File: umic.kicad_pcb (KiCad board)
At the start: 2 copper layers, 68.6 x 71.1 mm, 32 parts, among them J1 USB_B_Micro, J2 Conn_01x06, SW1 SW_MEC_5G, U1 LP38693MP-3.3, U2 STM32F302RBTx, Y1 32.768kHz, Y2 8MHz

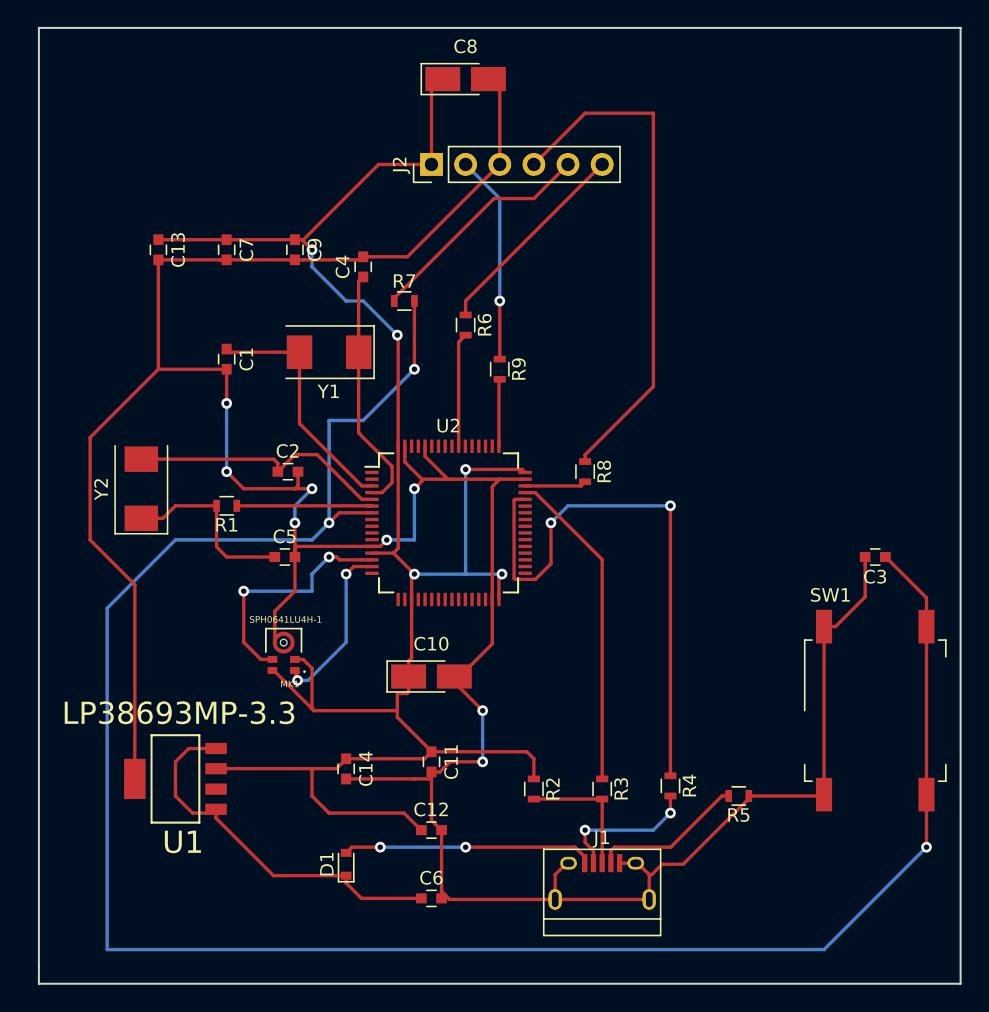
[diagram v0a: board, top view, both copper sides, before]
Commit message: take2: with ground plane
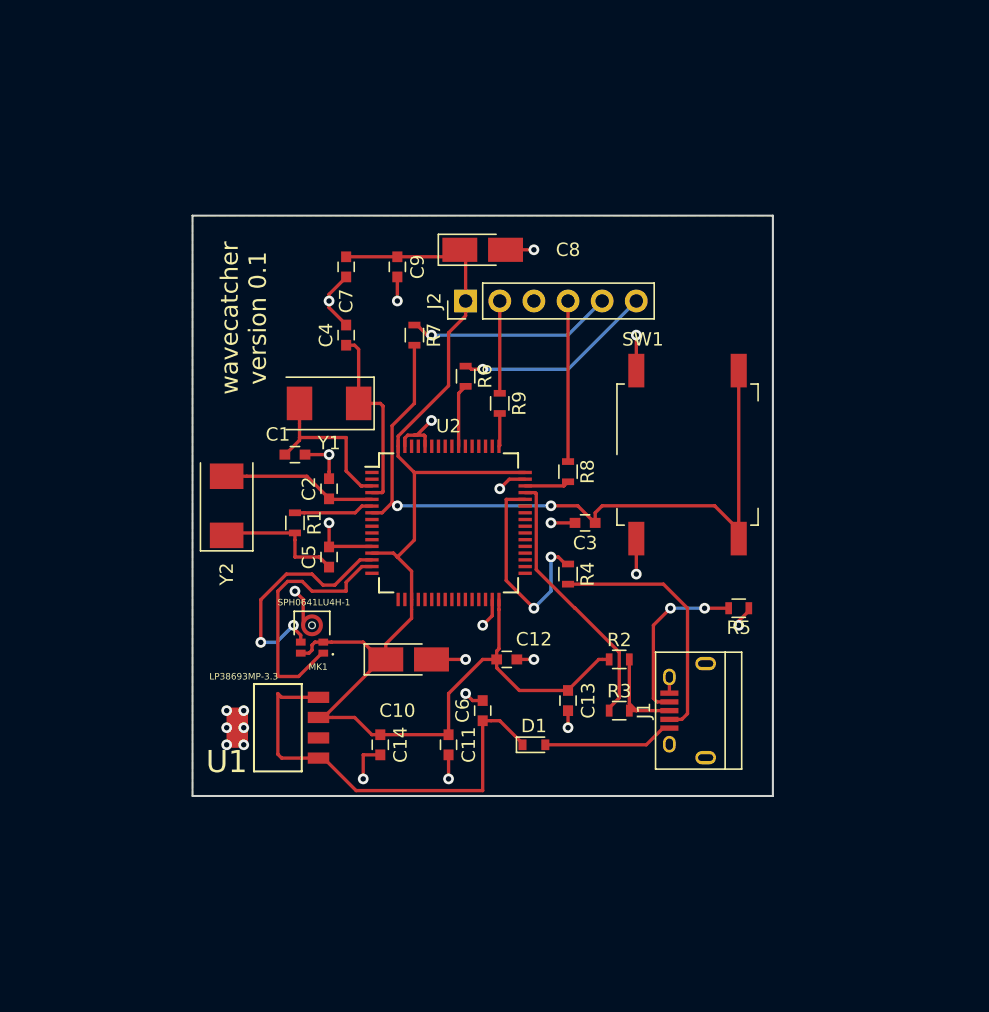
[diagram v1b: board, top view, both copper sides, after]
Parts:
- moved C13 45.3 mm to (57.1, 65.3)
- moved SW1 23.6 mm to (66.0, 47.0)
- moved C3 21.7 mm to (58.4, 52.1)
- moved R4 17.5 mm to (57.1, 55.9)
- moved D1 16.6 mm to (54.6, 68.6), turned to 0 degrees
- moved C6 14.5 mm to (50.8, 66.0), turned to 90 degrees
- moved J1 14.2 mm to (66.0, 66.0), turned to 90 degrees
- moved R5 14.0 mm to (69.8, 58.4)
- moved C12 13.9 mm to (52.6, 62.2)
- moved C8 12.8 mm to (50.8, 31.8)
- moved R2 11.5 mm to (61.0, 62.2), turned to 0 degrees
- moved J2 10.5 mm to (49.5, 35.6)
- moved C7 8.98 mm to (40.6, 33.0)
- moved C1 8.73 mm to (36.8, 47.0), turned to 0 degrees
- moved U1 8.52 mm to (35.6, 67.3)
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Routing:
- net GND: track 242.6 -> 50.3 mm, vias 8 -> 25
- net Net-(C3-Pad1): track 155.7 -> 55.5 mm, vias 3 -> 2
- net VDD: track 149.0 -> 101.2 mm, vias 5 -> 0
- net Net-(J2-Pad4): track 38.5 -> 11.9 mm
- net Net-(R4-Pad1): track 42.5 -> 16.2 mm
- net +5V: track 18.7 -> 9.74 mm, vias 2 -> 0
- net Net-(J2-Pad2): track 15.5 -> 6.87 mm, vias 1 -> 0
- net Net-(C2-Pad1): track 19.8 -> 11.5 mm
- net Net-(J1-Pad2): track 10.9 -> 19.0 mm, vias 2 -> 0
- net Net-(MK1-Pad1): track 13.1 -> 19.2 mm, vias 2 -> 0
- net Net-(C1-Pad1): track 18.1 -> 12.6 mm
- net Net-(C6-Pad1): track 28.4 -> 33.0 mm
- net Net-(R3-Pad1): track 24.1 -> 19.9 mm
- net Net-(R1-Pad1): track 10.1 -> 5.94 mm
- net Net-(C4-Pad1): track 18.3 -> 14.2 mm
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- added copper zone on B.Cu, net GND
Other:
- board size 68.6 x 71.1 mm -> 43.2 x 43.2 mm
- board text added: "wavecatcher version 0.1"

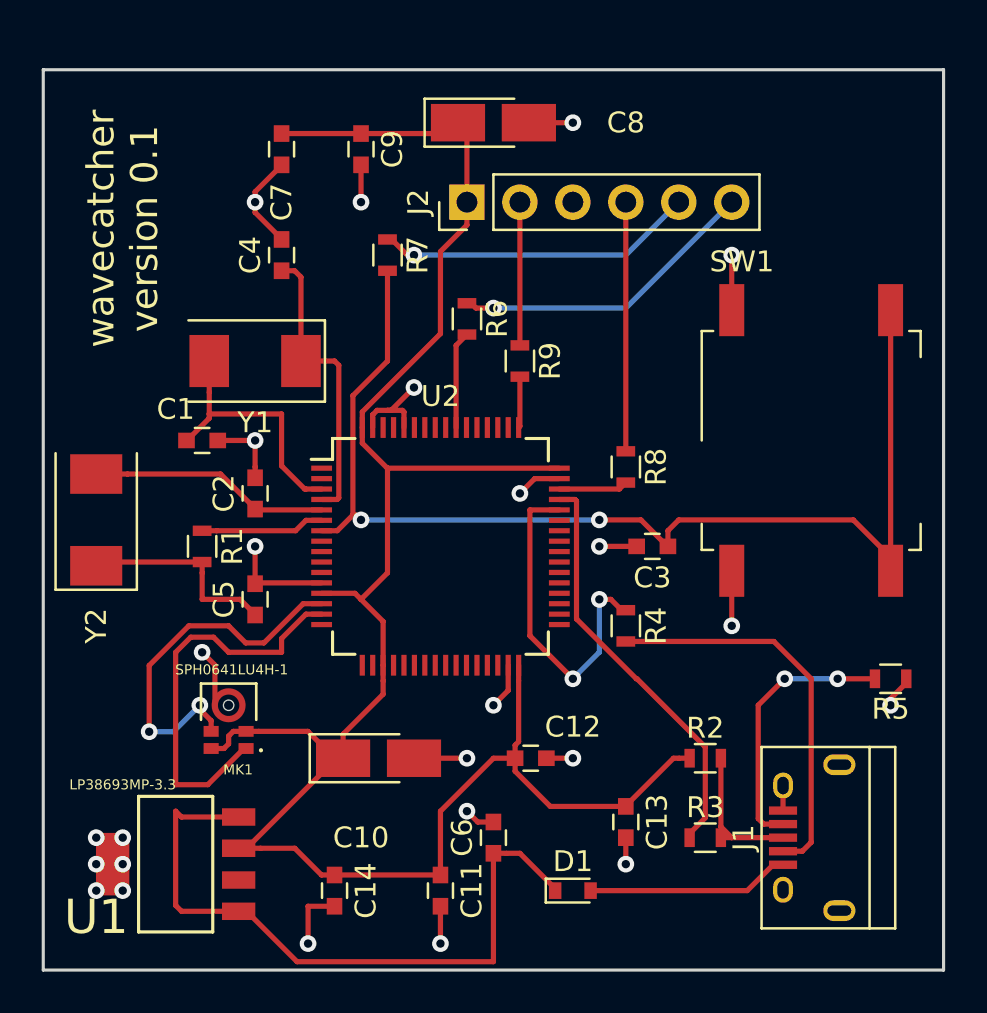
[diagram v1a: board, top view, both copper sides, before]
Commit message: added led
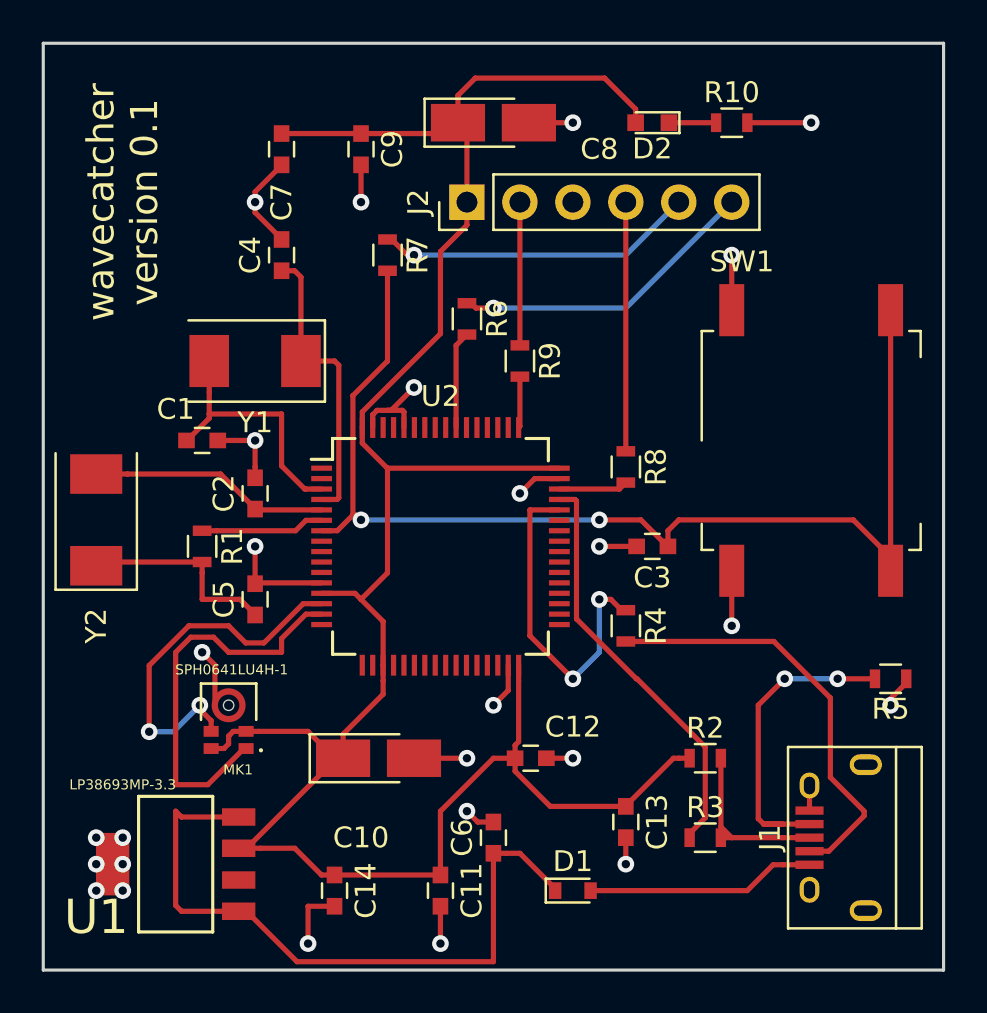
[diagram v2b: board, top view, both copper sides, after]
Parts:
- added D2: LED, LEDs:LED_0603, F.Cu at (58.4, 31.8)
- added R10: 68, Resistors_SMD:R_0603, F.Cu at (62.2, 31.8)
- moved J1 1.27 mm to (67.3, 66.0)
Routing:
- net VDD: track 101.2 -> 112.7 mm
- net GND: track 50.3 -> 53.3 mm, vias 25 -> 26
- net Net-(D2-Pad1): track 0.00 -> 2.26 mm
- net Net-(J1-Pad4): track 12.9 -> 15.1 mm
- net Net-(J1-Pad2): track 19.0 -> 20.6 mm
- net Net-(J1-Pad3): track 7.01 -> 8.28 mm
- net +5V: track 9.74 -> 11.0 mm
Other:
- board size 43.2 x 43.2 mm -> 43.2 x 44.5 mm

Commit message: sent off to fab
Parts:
- J1: footprint Connectors:USB_Micro-B -> Connectors:USB_Micro-B_10103594-0001LF
- Y1: footprint Crystals:Crystal_SMD_0603-2pin_6.0x3.5mm -> Crystals:Crystal_SMD_TXC_9HT11-2pin_2.0x1.2mm
- Y2: footprint Crystals:Crystal_SMD_0603-2pin_6.0x3.5mm -> Crystals:Crystal_SMD_Abracon_ABM3-2pin_5.0x3.2mm
- moved Y1 2.84 mm to (38.1, 40.6)
- moved Y2 1.27 mm to (33.0, 50.8)
- moved J1 0.69 mm to (68.0, 66.0)
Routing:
- net GND: track 53.3 -> 57.1 mm
- net Net-(C4-Pad1): track 14.2 -> 16.9 mm
- net Net-(C1-Pad1): track 12.6 -> 15.3 mm
- net Net-(C5-Pad1): track 9.81 -> 8.48 mm
- net Net-(C2-Pad1): track 11.5 -> 10.2 mm
- net Net-(J1-Pad2): track 20.6 -> 19.7 mm
- net Net-(J1-Pad3): track 8.28 -> 8.82 mm
- net +5V: track 11.0 -> 11.6 mm

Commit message: take2 at submitting to the fab
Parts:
- moved MK1 0.61 mm to (38.7, 59.7)
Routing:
- net Net-(MK1-Pad1): track 19.2 -> 8.50 mm
- net Net-(MK1-Pad4): track 17.8 -> 12.4 mm, vias 2 -> 0
- net VDD: track 112.7 -> 114.4 mm
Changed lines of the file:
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@@
     (thickness 1.6)
     (drawings 5)
-    (tracks 294)
+    (tracks 283)
     (zones 0)
     (modules 34)
@@
   )
   (module SPH0641LU4H-1:MIC_SPH0641LU4H-1 (layer F.Cu)
-    (at 38.1 59.69 180)
+    (at 38.71375 59.7025 180)
     (attr smd)
     (fp_text reference MK1 (at -0.452726 -3.09295 180) (layer F.SilkS)
@@
   (segment (start 39.37 53.86) (end 39.37 52.07) (width 0.25) (layer F.Cu) (net 2))
   (via (at 39.37 52.07) (size 0.8) (drill 0.4) (layers F.Cu B.Cu) (net 2))
-  (segment (start 37.44375 59.7025) (end 37.44375 57.76375) (width 0.25) (layer F.Cu) (net 2))
-  (via (at 36.83 57.15) (size 0.8) (drill 0.4) (layers F.Cu B.Cu) (net 2))
-  (segment (start 37.44375 57.76375) (end 36.83 57.15) (width 0.25) (layer F.Cu) (net 2))
   (via (at 31.75 66.04) (size 0.8) (drill 0.4) (layers F.Cu B.Cu) (net 2))
   (via (at 31.75 67.31) (size 0.8) (drill 0.4) (layers F.Cu B.Cu) (net 2))
@@
   (segment (start 38.5826 69.5706) (end 35.8394 69.5706) (width 0.25) (layer F.Cu) (net 7))
   (segment (start 35.8394 69.5706) (end 35.56 69.2912) (width 0.25) (layer F.Cu) (net 7))
-  (segment (start 39.55 60.942) (end 38.9375 60.942) (width 0.25) (layer F.Cu) (net 8))
-  (segment (start 41.902 60.942) (end 39.55 60.942) (width 0.25) (layer F.Cu) (net 8))
-  (segment (start 43.19 62.23) (end 41.902 60.942) (width 0.25) (layer F.Cu) (net 8))
   (segment (start 43.59 62.23) (end 43.19 62.23) (width 0.25) (layer F.Cu) (net 8))
   (segment (start 43.2816 62.23) (end 43.59 62.23) (width 0.25) (layer F.Cu) (net 8))
@@
   (segment (start 52.01 61.435) (end 52.01 58.52) (width 0.25) (layer F.Cu) (net 8))
   (segment (start 51.84 62.23) (end 51.84 61.605) (width 0.25) (layer F.Cu) (net 8))
-  (segment (start 37.875 61.764) (end 38.1 61.539) (width 0.25) (layer F.Cu) (net 8))
-  (segment (start 37.2625 61.764) (end 37.875 61.764) (width 0.25) (layer F.Cu) (net 8))
-  (segment (start 38.325 60.942) (end 38.9375 60.942) (width 0.25) (layer F.Cu) (net 8))
-  (segment (start 38.1 61.167) (end 38.325 60.942) (width 0.25) (layer F.Cu) (net 8))
-  (segment (start 38.1 61.539) (end 38.1 61.167) (width 0.25) (layer F.Cu) (net 8))
   (segment (start 40.64 32.27) (end 44.45 32.27) (width 0.25) (layer F.Cu) (net 8))
   (segment (start 48.58 32.27) (end 49.1 31.75) (width 0.25) (layer F.Cu) (net 8))
@@
   (segment (start 64.69 66.04) (end 62.23 66.04) (width 0.25) (layer F.Cu) (net 11))
   (segment (start 52.07 42.43) (end 52.07 35.56) (width 0.25) (layer F.Cu) (net 13))
-  (segment (start 38.836 61.764) (end 37.1 63.5) (width 0.25) (layer F.Cu) (net 14))
-  (segment (start 38.9375 61.764) (end 38.836 61.764) (width 0.25) (layer F.Cu) (net 14))
-  (segment (start 37.1 63.5) (end 35.56 63.5) (width 0.25) (layer F.Cu) (net 14))
-  (segment (start 35.56 63.5) (end 35.56 57.15) (width 0.25) (layer F.Cu) (net 14))
-  (segment (start 35.56 57.15) (end 36.285001 56.424999) (width 0.25) (layer F.Cu) (net 14))
-  (segment (start 36.285001 56.424999) (end 37.374999 56.424999) (width 0.25) (layer F.Cu) (net 14))
-  (segment (start 37.374999 56.424999) (end 38.1 57.15) (width 0.25) (layer F.Cu) (net 14))
-  (segment (start 38.1 57.15) (end 40.64 57.15) (width 0.25) (layer F.Cu) (net 14))
-  (segment (start 41.81 55.32) (end 42.56 55.32) (width 0.25) (layer F.Cu) (net 14))
-  (segment (start 40.64 56.49) (end 41.81 55.32) (width 0.25) (layer F.Cu) (net 14))
-  (segment (start 40.64 57.15) (end 40.64 56.49) (width 0.25) (layer F.Cu) (net 14))
   (segment (start 41.67359 54.82) (end 39.7936 56.69999) (width 0.25) (layer F.Cu) (net 15))
   (segment (start 42.56 54.82) (end 41.67359 54.82) (width 0.25) (layer F.Cu) (net 15))
   (segment (start 39.7936 56.69999) (end 38.91999 56.69999) (width 0.25) (layer F.Cu) (net 15))
   (segment (start 38.91999 56.69999) (end 38.1 55.88) (width 0.25) (layer F.Cu) (net 15))
-  (segment (start 36.19359 55.88) (end 34.29 57.78359) (width 0.25) (layer F.Cu) (net 15))
-  (segment (start 38.1 55.88) (end 36.19359 55.88) (width 0.25) (layer F.Cu) (net 15))
-  (segment (start 34.29 57.78359) (end 34.29 60.96) (width 0.25) (layer F.Cu) (net 15))
-  (via (at 34.29 60.96) (size 0.8) (drill 0.4) (layers F.Cu B.Cu) (net 15))
-  (segment (start 37.2625 60.431) (end 36.83 59.9985) (width 0.25) (layer F.Cu) (net 15))
-  (segment (start 37.2625 60.942) (end 37.2625 60.431) (width 0.25) (layer F.Cu) (net 15))
-  (via (at 36.71875 59.69) (size 0.8) (drill 0.4) (layers F.Cu B.Cu) (net 15))
-  (segment (start 36.83 59.9985) (end 36.83 59.80125) (width 0.25) (layer F.Cu) (net 15))
-  (segment (start 36.83 59.80125) (end 36.71875 59.69) (width 0.25) (layer F.Cu) (net 15))
-  (segment (start 35.44875 60.96) (end 34.29 60.96) (width 0.25) (layer B.Cu) (net 15))
-  (segment (start 36.71875 59.69) (end 35.44875 60.96) (width 0.25) (layer B.Cu) (net 15))
   (segment (start 37.53 51.32) (end 36.83 51.32) (width 0.25) (layer F.Cu) (net 16))
   (segment (start 41.81 50.82) (end 41.31 51.32) (width 0.25) (layer F.Cu) (net 16))
@@
   (segment (start 69.62 68.53) (end 69.38 68.77) (width 0.25) (layer F.Cu) (net 2))
   (segment (start 69.62 67) (end 69.62 68.53) (width 0.25) (layer F.Cu) (net 2))
+  (segment (start 38.0575 59.715) (end 38.0575 59.415) (width 0.25) (layer F.Cu) (net 2))
+  (via (at 38.1 57.15) (size 0.8) (drill 0.4) (layers F.Cu B.Cu) (net 2))
+  (segment (start 38.0575 57.1925) (end 38.1 57.15) (width 0.25) (layer F.Cu) (net 2))
+  (segment (start 38.0575 59.715) (end 38.0575 57.1925) (width 0.25) (layer F.Cu) (net 2))
   (segment (start 39.37 50.255) (end 39.37 50.28) (width 0.25) (layer F.Cu) (net 3))
   (segment (start 37.865 48.75) (end 39.37 50.255) (width 0.25) (layer F.Cu) (net 3))
@@
   (segment (start 49.1 30.44002) (end 49.1 31.75) (width 0.25) (layer F.Cu) (net 8))
   (segment (start 49.93001 29.61001) (end 49.1 30.44002) (width 0.25) (layer F.Cu) (net 8))
+  (segment (start 39.54575 60.96) (end 39.55125 60.9545) (width 0.25) (layer F.Cu) (net 8))
+  (segment (start 39.159248 60.96) (end 39.54575 60.96) (width 0.25) (layer F.Cu) (net 8))
+  (segment (start 38.342748 61.7765) (end 39.159248 60.96) (width 0.25) (layer F.Cu) (net 8))
+  (segment (start 37.87625 61.7765) (end 38.342748 61.7765) (width 0.25) (layer F.Cu) (net 8))
+  (segment (start 43.59 62.23) (end 42.04 62.23) (width 0.25) (layer F.Cu) (net 8))
+  (segment (start 37.97775 61.7765) (end 37.87625 61.7765) (width 0.25) (layer F.Cu) (net 8))
+  (segment (start 41.10125 63.16875) (end 42.04 62.23) (width 0.25) (layer F.Cu) (net 8))
+  (segment (start 39.37 63.16875) (end 41.10125 63.16875) (width 0.25) (layer F.Cu) (net 8))
+  (segment (start 39.37 63.16875) (end 37.97775 61.7765) (width 0.25) (layer F.Cu) (net 8))
   (segment (start 64.215 67.34) (end 66.5 67.34) (width 0.25) (layer F.Cu) (net 9))
   (segment (start 63.765 65.39) (end 63.5 65.125) (width 0.25) (layer F.Cu) (net 10))
@@
   (segment (start 67.575 66.69) (end 67.650001 66.614999) (width 0.25) (layer F.Cu) (net 12))
   (segment (start 66.5 66.69) (end 67.575 66.69) (width 0.25) (layer F.Cu) (net 12))
+  (segment (start 40.16375 61.7765) (end 40.64 61.30025) (width 0.25) (layer F.Cu) (net 14))
+  (segment (start 39.55125 61.7765) (end 40.16375 61.7765) (width 0.25) (layer F.Cu) (net 14))
+  (segment (start 41.81 55.32) (end 42.56 55.32) (width 0.25) (layer F.Cu) (net 14))
+  (segment (start 40.64 56.49) (end 41.81 55.32) (width 0.25) (layer F.Cu) (net 14))
+  (segment (start 40.64 61.30025) (end 40.64 56.49) (width 0.25) (layer F.Cu) (net 14))
+  (segment (start 37.87625 60.9545) (end 37.77475 60.9545) (width 0.25) (layer F.Cu) (net 15))
+  (segment (start 37.77475 60.9545) (end 36.83 60.00975) (width 0.25) (layer F.Cu) (net 15))
+  (segment (start 36.83 60.00975) (end 36.83 55.88) (width 0.25) (layer F.Cu) (net 15))
+  (segment (start 36.83 55.88) (end 38.1 55.88) (width 0.25) (layer F.Cu) (net 15))
   (segment (start 60.21 65.84) (end 60.96 65.09) (width 0.25) (layer F.Cu) (net 17))
   (segment (start 60.21 66.04) (end 60.21 65.84) (width 0.25) (layer F.Cu) (net 17))

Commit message: take3, connect mic to spi pins
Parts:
- moved MK1 7.44 mm to (45.7, 62.2)
- moved C10 7.30 mm to (38.1, 61.0), turned to 180 degrees
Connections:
- U2 pad 14: Net-(MK1-Pad4) -> Net-(U2-Pad14)
- U2 pad 15: Net-(MK1-Pad1) -> Net-(U2-Pad15)
- U2 pad 21: Net-(U2-Pad21) -> Net-(MK1-Pad4)
- U2 pad 22: Net-(U2-Pad22) -> Net-(MK1-Pad1)
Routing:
- net Net-(MK1-Pad4): track 12.4 -> 10.5 mm
- net VDD: track 114.4 -> 113.1 mm
- net GND: track 57.1 -> 56.3 mm
